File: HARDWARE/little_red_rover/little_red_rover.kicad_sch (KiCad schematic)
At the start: 38 parts, among them J1 USB_C_Receptacle_USB2.0_14P, J2 Conn_01x04_Socket, J3 Conn_01x02_Socket, J4 Conn_01x02_Socket, U1 ESP32-C3-MINI-1, U2 BQ24230RGT, U3 MIC5504-3.3YM5, U4 MIC2876-5.0YMT-TR, U5 DRV8212P, U6 DRV8212P, U7 GP1S094HCZ0F, U8 GP1S094HCZ0F

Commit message: v1.0 board layout
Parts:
- added R14, R15: 10k, Capacitor_SMD:C_0603_1608Metric_Pad1.08x0.95mm_HandSolder, symbol Device:R
- added U9: LSM6DS3, Package_LGA:LGA-14_3x2.5mm_P0.5mm_LayoutBorder3x4y, symbol Sensor_Motion:LSM6DS3
- BT1: footprint digikey_imports:18650_holder -> Battery:BatteryHolder_MPD_BH-18650-PC2
- C1, C3, C4: JLC (none) -> 0603; LCSC (none) -> C15849
- C2, C5, C6: JLC (none) -> 0603; LCSC (none) -> C19666
- D1, D2: JLC (none) -> 0603; LCSC (none) -> C5342734
- D3, D4, D5: JLC (none) -> SMD,2x2mm; LCSC (none) -> C965555
- J1: footprint Connector_USB:USB_C_Receptacle_GCT_USB4135-GF-A_6P_TopMnt_Horizontal -> Connector_USB:USB_C_Receptacle_GCT_USB4105-xx-A_16P_TopMnt_Horizontal; JLC (none) -> SMD; LCSC (none) -> C2927038
- J2: JLC (none) -> SMD,P=1.25mm; LCSC (none) -> C189895
- L1: JLC (none) -> 1008; LCSC (none) -> C139491
- R1, R10, R11, R12, R13, R2, R3, R4, R5, R6, R7, R8, R9: JLC (none) -> 0603
- U1: JLC (none) -> -; LCSC (none) -> C5290152
- U2: JLC (none) -> VQFN-16-EP(3x3); LCSC (none) -> C138361
- U3: JLC (none) -> SOT-23-5; LCSC (none) -> C88419
- U4: JLC (none) -> UDFN-8-EP(2x2); LCSC (none) -> C621881
- U5, U6: JLC (none) -> WSON-8(2x2); LCSC (none) -> C5208051
- U7, U8: JLC (none) -> DIP-4; LCSC (none) -> C920601
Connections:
- net +3.3V: now also R14.1, R15.1, U9.1 (SDO/SA0), U9.12 (CS), U9.5 (VDDIO), U9.8 (VDD)
- net +5V: no longer C1.1, J1.A4 (VBUS), J1.A9 (VBUS), J1.B4 (VBUS), J1.B9 (VBUS), U2.13 (IN)
- net GND: now also U9.6 (GND), U9.7 (GND)
- net imu_scl: now reaches U1.5 (GPIO2/ADC1_CH2)
- net imu_scl: now also R15.2, U9.13 (SCL)
- net imu_sda: now reaches U1.6 (GPIO3/ADC1_CH3)
- net imu_sda: now also R14.2, U9.14 (SDA)
- new net usb_5v: C1.1, J1.A4 (VBUS), J1.A9 (VBUS), J1.B4 (VBUS), J1.B9 (VBUS), U2.13 (IN)
- no-connect marks 0 -> 4
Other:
- note added: "Gyro + Accel"
- moved on the sheet: J3, J4, R10, R11, R12, U1, U5, U6, U7, U8

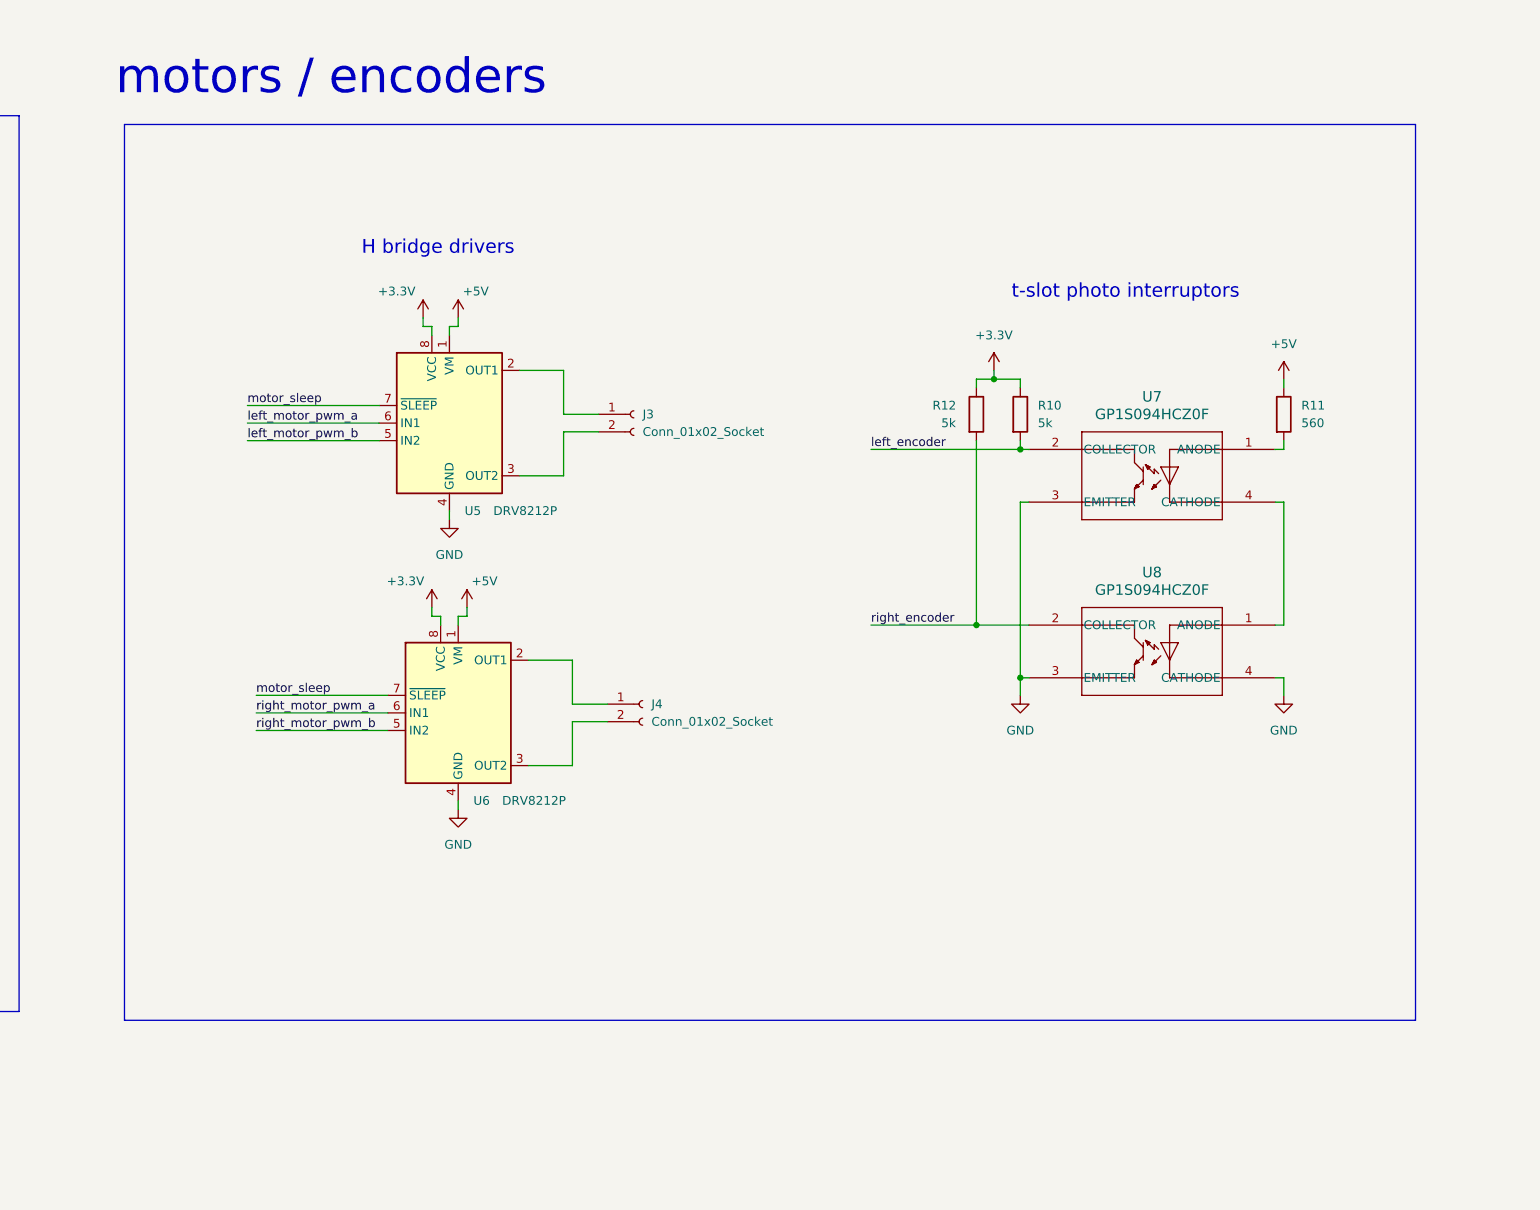
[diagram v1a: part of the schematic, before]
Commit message: Update pcb outline, add threaded inserts
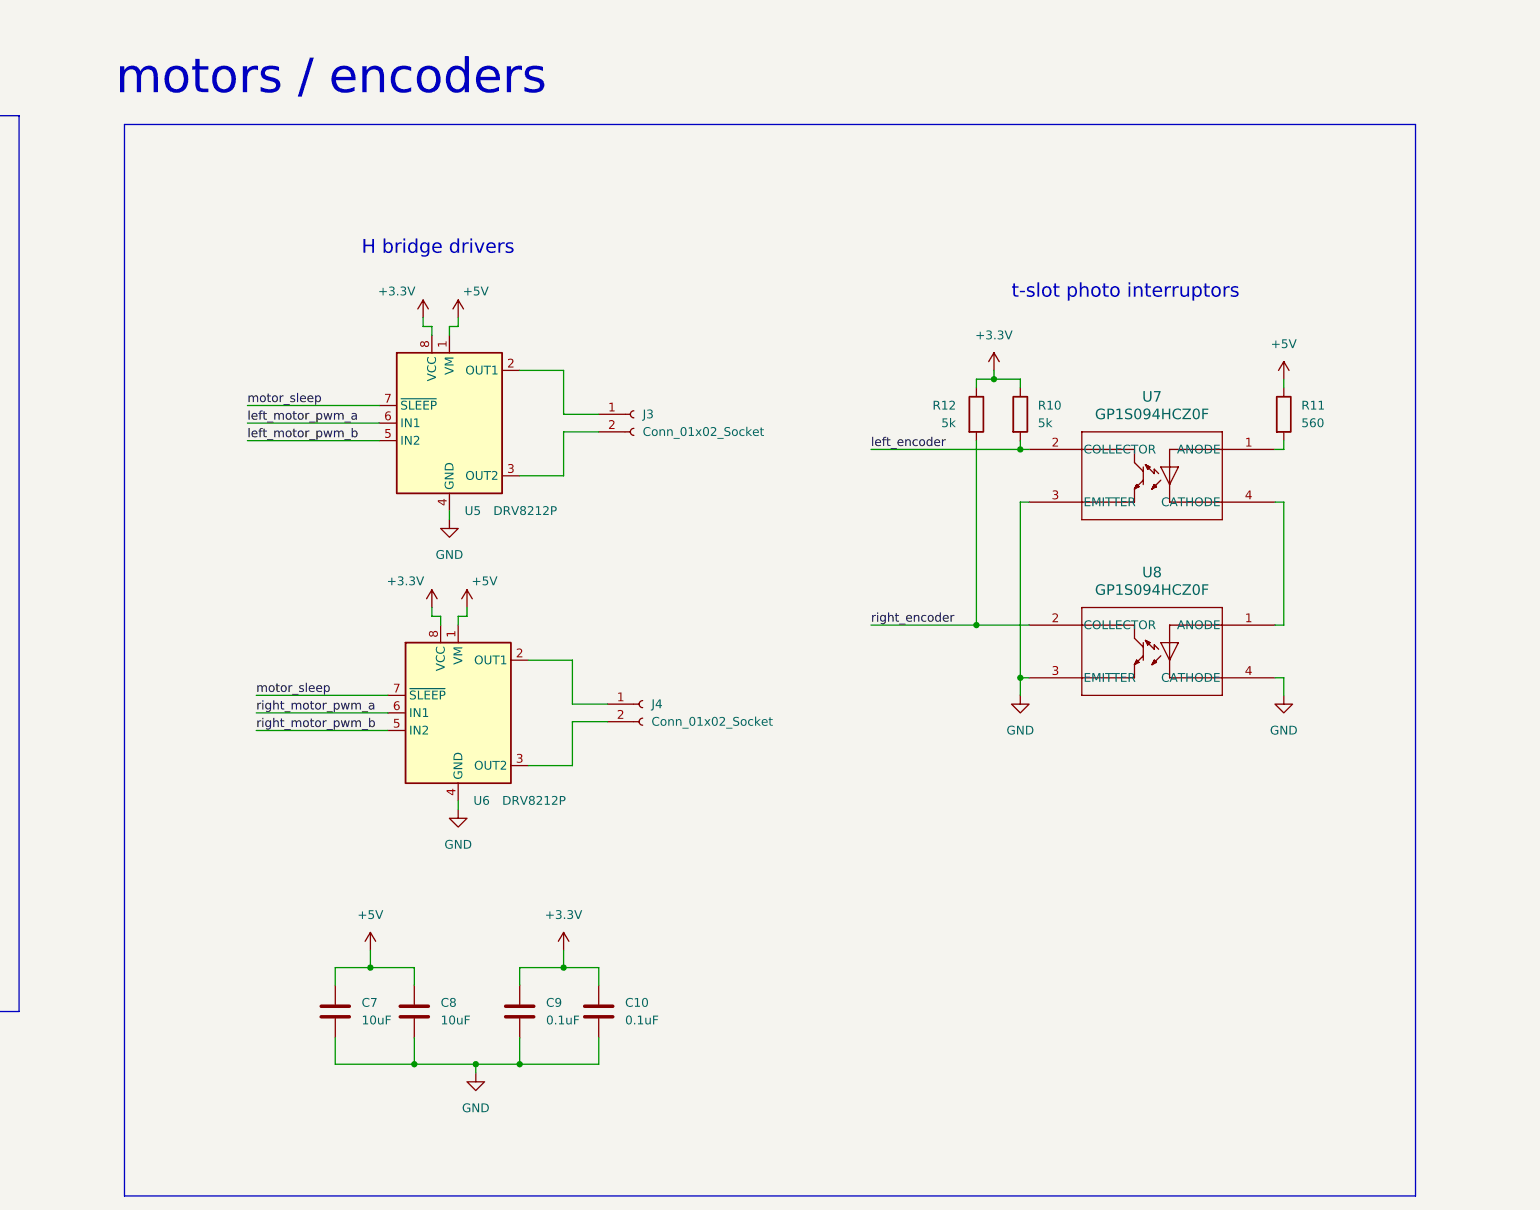
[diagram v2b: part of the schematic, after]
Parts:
- added C10, C9: 0.1uF, Capacitor_SMD:C_0603_1608Metric_Pad1.08x0.95mm_HandSolder, symbol Device:C
- added C7, C8: 10uF, Capacitor_SMD:C_0603_1608Metric_Pad1.08x0.95mm_HandSolder, symbol Device:C
- BT1: footprint Battery:BatteryHolder_MPD_BH-18650-PC2 -> digikey_imports:18650_holder
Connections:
- net +3.3V: now also C10.1, C9.1
- net +5V: now also C7.1, C8.1
- net GND: now also C10.2, C7.2, C8.2, C9.2

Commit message: Layout fixes + added QR code
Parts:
- removed BT1: Battery_Cell, digikey_imports:18650_holder, symbol Device:Battery_Cell
- added H1, H2, H3: MountingHole, digikey_imports:m3_threaded_insert, symbol Mechanical:MountingHole
- added J5, J6: Conn_01x01_Socket, digikey_imports:18650_holder, symbol Connector:Conn_01x01_Socket
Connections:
- net GND: now also J5.1 (Pin_1)
- net at C5.1, U2.2 (BAT), U2.3 (BAT): now also J6.1 (Pin_1)
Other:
- moved on the sheet: R14, R15, U9

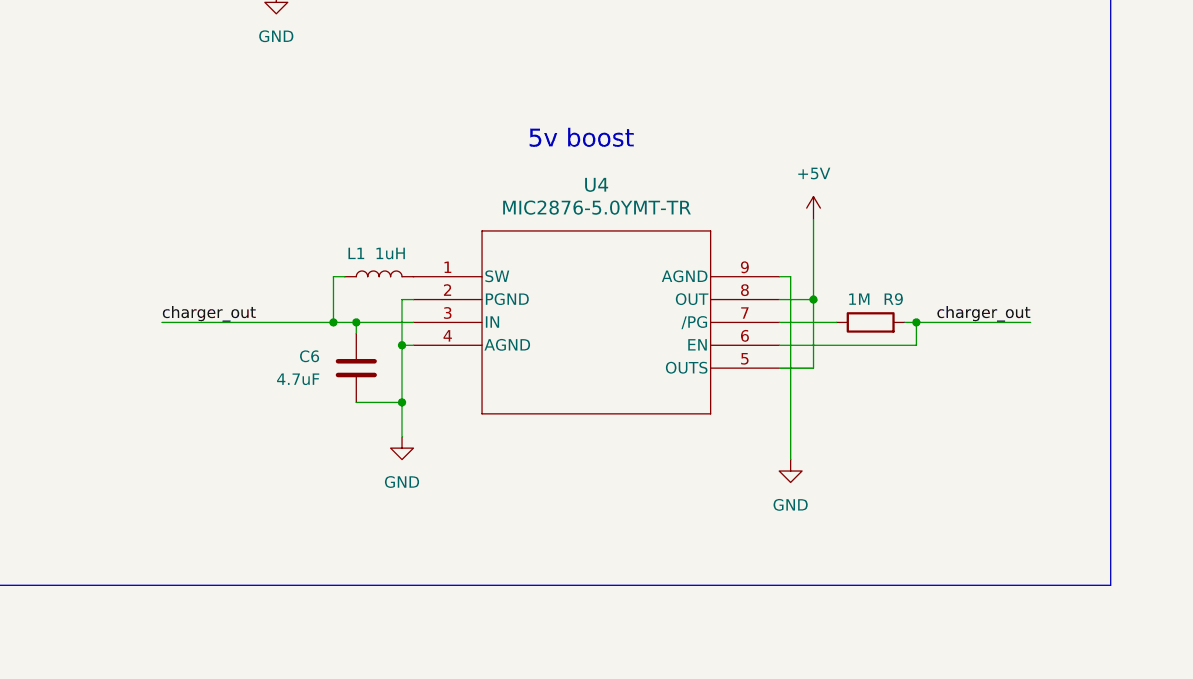
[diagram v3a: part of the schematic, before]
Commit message: Change 5v boost converter due to shortage
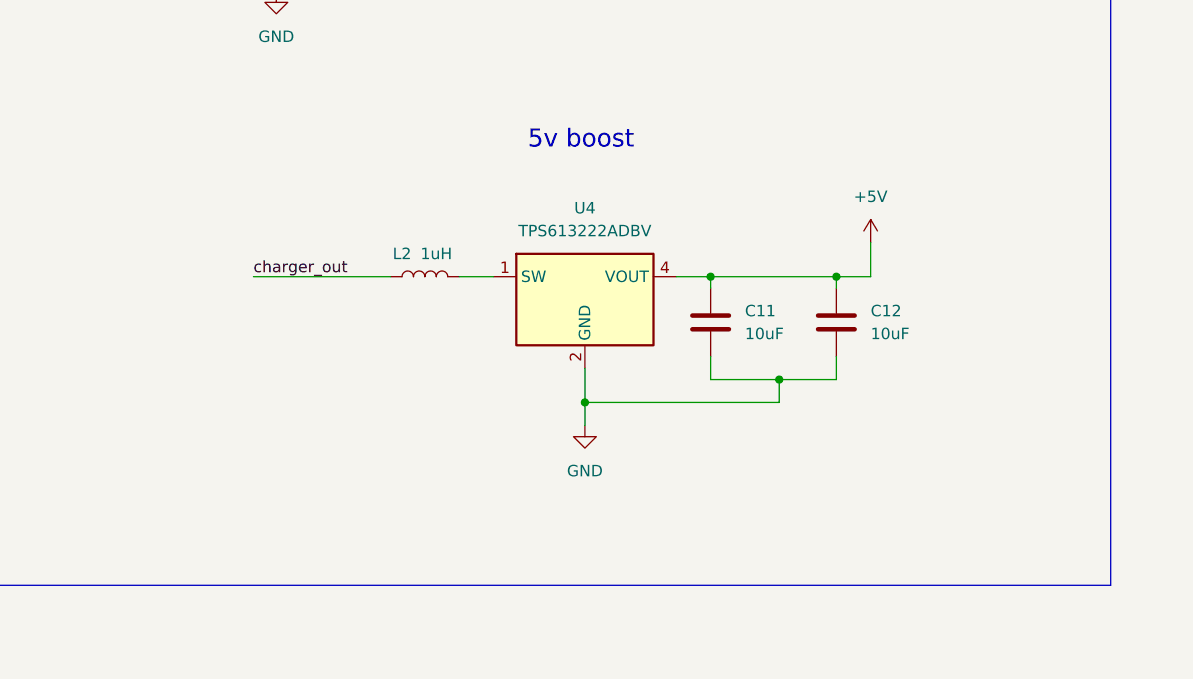
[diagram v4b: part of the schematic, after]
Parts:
- removed C6: 4.7uF, Capacitor_SMD:C_0603_1608Metric_Pad1.08x0.95mm_HandSolder, symbol Device:C
- removed L1: 1uH, Inductor_SMD:L_1008_2520Metric_Pad1.43x2.20mm_HandSolder, symbol Device:L
- removed R9: 1M, Resistor_SMD:R_0603_1608Metric_Pad0.98x0.95mm_HandSolder, symbol Device:R
- removed U4: MIC2876-5.0YMT-TR, digikey_imports:UDFN8_2X2_MCH-L, symbol digikey_imports:MIC2876-5.0YMT-TR
- added C11, C12: 10uF, Capacitor_SMD:C_0603_1608Metric_Pad1.08x0.95mm_HandSolder, symbol Device:C
- added L2: 1uH, Inductor_SMD:L_1008_2520Metric_Pad1.43x2.20mm_HandSolder, symbol Device:L
- added U4: TPS613222ADBV, Package_TO_SOT_SMD:SOT-23-5, symbol Regulator_Switching:TPS613222ADBV
- C1, C3, C4: LCSC C15849 -> (none)
- C10, C7, C8, C9: JLC (none) -> 0603
- C2, C5: LCSC C19666 -> (none)
- H1, H2, H3: JLC (none) -> -; LCSC (none) -> C5301780
- J3, J4: JLC (none) -> Push-Pull,P=2.54mm; LCSC (none) -> C2932679
- J5, J6: JLC (none) -> SMD; LCSC (none) -> C2979182
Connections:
- net +5V: now also C11.1, C12.1, U4.4 (VOUT)
- net GND: now also C11.2, C12.2, U4.2 (GND)
- net charger_out: now also L2.1
- new net: L2.2, U4.1 (SW)

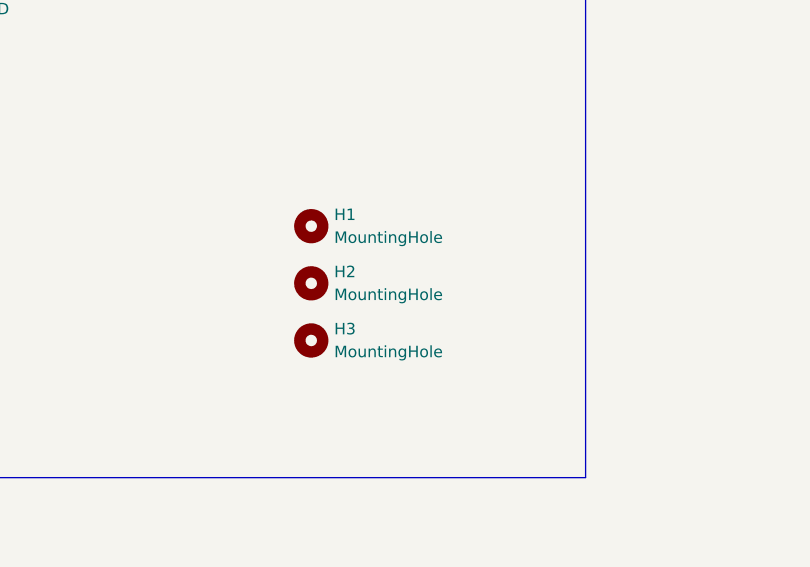
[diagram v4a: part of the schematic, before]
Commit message: Fix threaded inserts not being included in BOM / placement
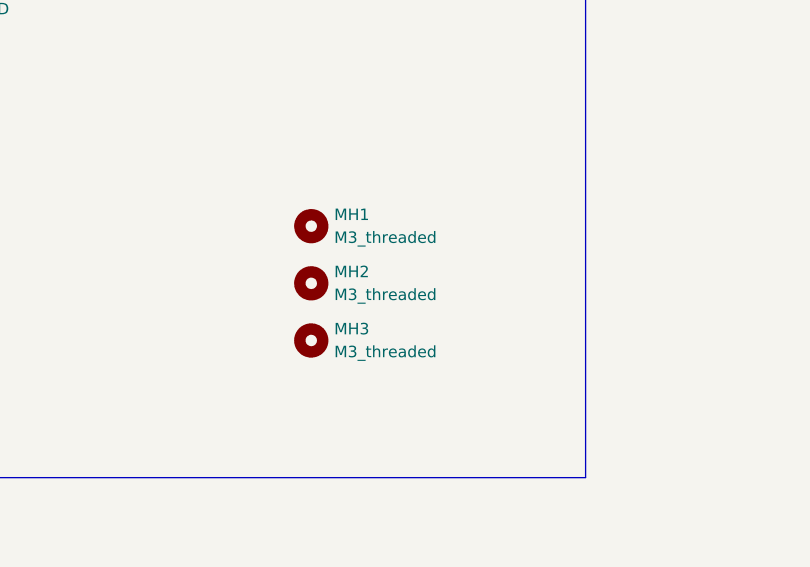
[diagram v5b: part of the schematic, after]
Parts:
- MH1: renamed from H1; value MountingHole -> M3_threaded
- MH2: renamed from H2; value MountingHole -> M3_threaded
- MH3: renamed from H3; value MountingHole -> M3_threaded
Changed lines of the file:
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@@
   (symbol (lib_id "Mechanical:MountingHole") (at 354.33 144.78 0) (unit 1)
     (in_bom yes) (on_board yes) (dnp no) (fields_autoplaced)
-    (property "Reference" "H2" (at 356.87 143.51 0)
-      (effects (font (size 1.27 1.27)) (justify left))
-    )
-    (property "Value" "MountingHole" (at 356.87 146.05 0)
+    (property "Reference" "MH2" (at 356.87 143.51 0)
+      (effects (font (size 1.27 1.27)) (justify left))
+    )
+    (property "Value" "M3_threaded" (at 356.87 146.05 0)
       (effects (font (size 1.27 1.27)) (justify left))
     )
@@
       (project "little_red_rover"
         (path "/6f482c50-19c8-43f6-b4b5-8739f6fb7866"
-          (reference "H2") (unit 1)
+          (reference "MH2") (unit 1)
         )
       )
@@
   (symbol (lib_id "Mechanical:MountingHole") (at 354.33 151.13 0) (unit 1)
     (in_bom yes) (on_board yes) (dnp no) (fields_autoplaced)
-    (property "Reference" "H3" (at 356.87 149.86 0)
-      (effects (font (size 1.27 1.27)) (justify left))
-    )
-    (property "Value" "MountingHole" (at 356.87 152.4 0)
+    (property "Reference" "MH3" (at 356.87 149.86 0)
+      (effects (font (size 1.27 1.27)) (justify left))
+    )
+    (property "Value" "M3_threaded" (at 356.87 152.4 0)
       (effects (font (size 1.27 1.27)) (justify left))
     )
@@
       (project "little_red_rover"
         (path "/6f482c50-19c8-43f6-b4b5-8739f6fb7866"
-          (reference "H3") (unit 1)
+          (reference "MH3") (unit 1)
         )
       )
@@
   (symbol (lib_id "Mechanical:MountingHole") (at 354.33 138.43 0) (unit 1)
     (in_bom yes) (on_board yes) (dnp no) (fields_autoplaced)
-    (property "Reference" "H1" (at 356.87 137.16 0)
-      (effects (font (size 1.27 1.27)) (justify left))
-    )
-    (property "Value" "MountingHole" (at 356.87 139.7 0)
+    (property "Reference" "MH1" (at 356.87 137.16 0)
+      (effects (font (size 1.27 1.27)) (justify left))
+    )
+    (property "Value" "M3_threaded" (at 356.87 139.7 0)
       (effects (font (size 1.27 1.27)) (justify left))
     )
@@
       (project "little_red_rover"
         (path "/6f482c50-19c8-43f6-b4b5-8739f6fb7866"
-          (reference "H1") (unit 1)
-        )
-      )
+          (reference "MH1") (unit 1)
+        )
+      )
